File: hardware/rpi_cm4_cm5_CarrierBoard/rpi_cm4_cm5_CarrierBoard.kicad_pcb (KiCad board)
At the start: 2 copper layers, 181.6 x 100.6 mm, 489 parts, among them J1 DM3AT-SF-PEJM5, J19 RPI_CMx_A, J2 0484050003, J3 0484050003, J4 2086581001, J5 0826-1X1T-32-F, J6 M20-9990245, J7 2998TR, J8 62684-402100ALF, J9 5051101092, Q1 2N7002, Q10 SSM3K56FS,LF, Q11 SSM3K56FS,LF, Q12 2N7002, Q13 2N7002, Q14 2N7002, Q15 2N7002, Q16 BCP56-16, Q17 ISP75DP06LMXTSA1, Q18 MMBT3904-7-F, Q2 2N7002, Q3 2N7002, Q4 2N7002, Q5 2N7002, Q6 2N7002, Q7 2N7002, Q8 2N7002, Q9 IPD60R360P7ATMA1, U1 STM6710DWB6F, U10 TPS54527DDAR, U11 TPS54527DDAR, U12 TPS7A7001DDAR, U13 SE555DR, U14 SN74LVC1G14DBVR, U15 SN65DSI84ZXHR, U16 SN74LVC1G125DBVR, U17 RPI_CMx_B, U18 AP22913W6-7, U19 SN74LVC1G125DBVR, U2 SN74LVC1G125DBVR, U20 SN74LVC1G07DBVR, U21 MCP7940NT-I/MS, U22 FSUSB42UMX, U23 LTC4359IDCB, U24 MAX16928CGUP, U25 TPS79901DRVR, U26 TPS61169DCKR, U27 AP22913W6-7, U28 DSPIC33EP512MU810-I/PT, U3 SN74LVC1G125DBVR, U4 AP22913W6-7, U5 SN74LVC1G125DBVR, U6 SST25VF512A, U7 UPD720202K8-711-BAA-A, U8 AP2192AFGEG-7, U9 TPS54527DDAR, Y1 24MHz, Y2 32.768kHz

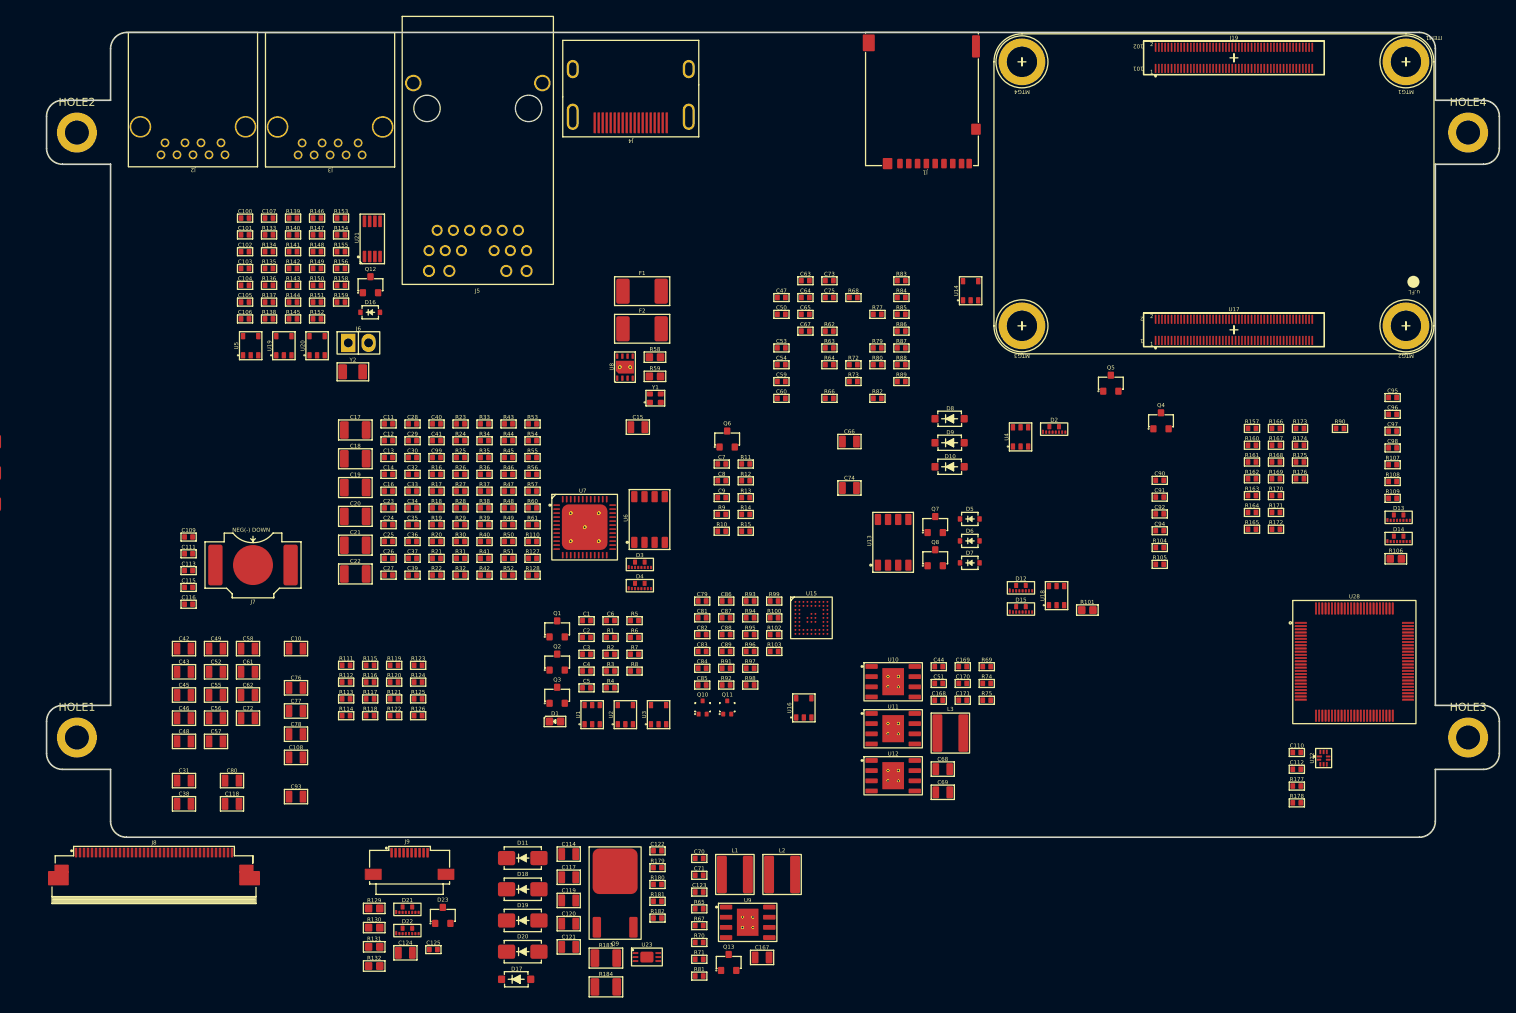
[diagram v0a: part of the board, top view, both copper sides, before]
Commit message: Add dsPIC sheet
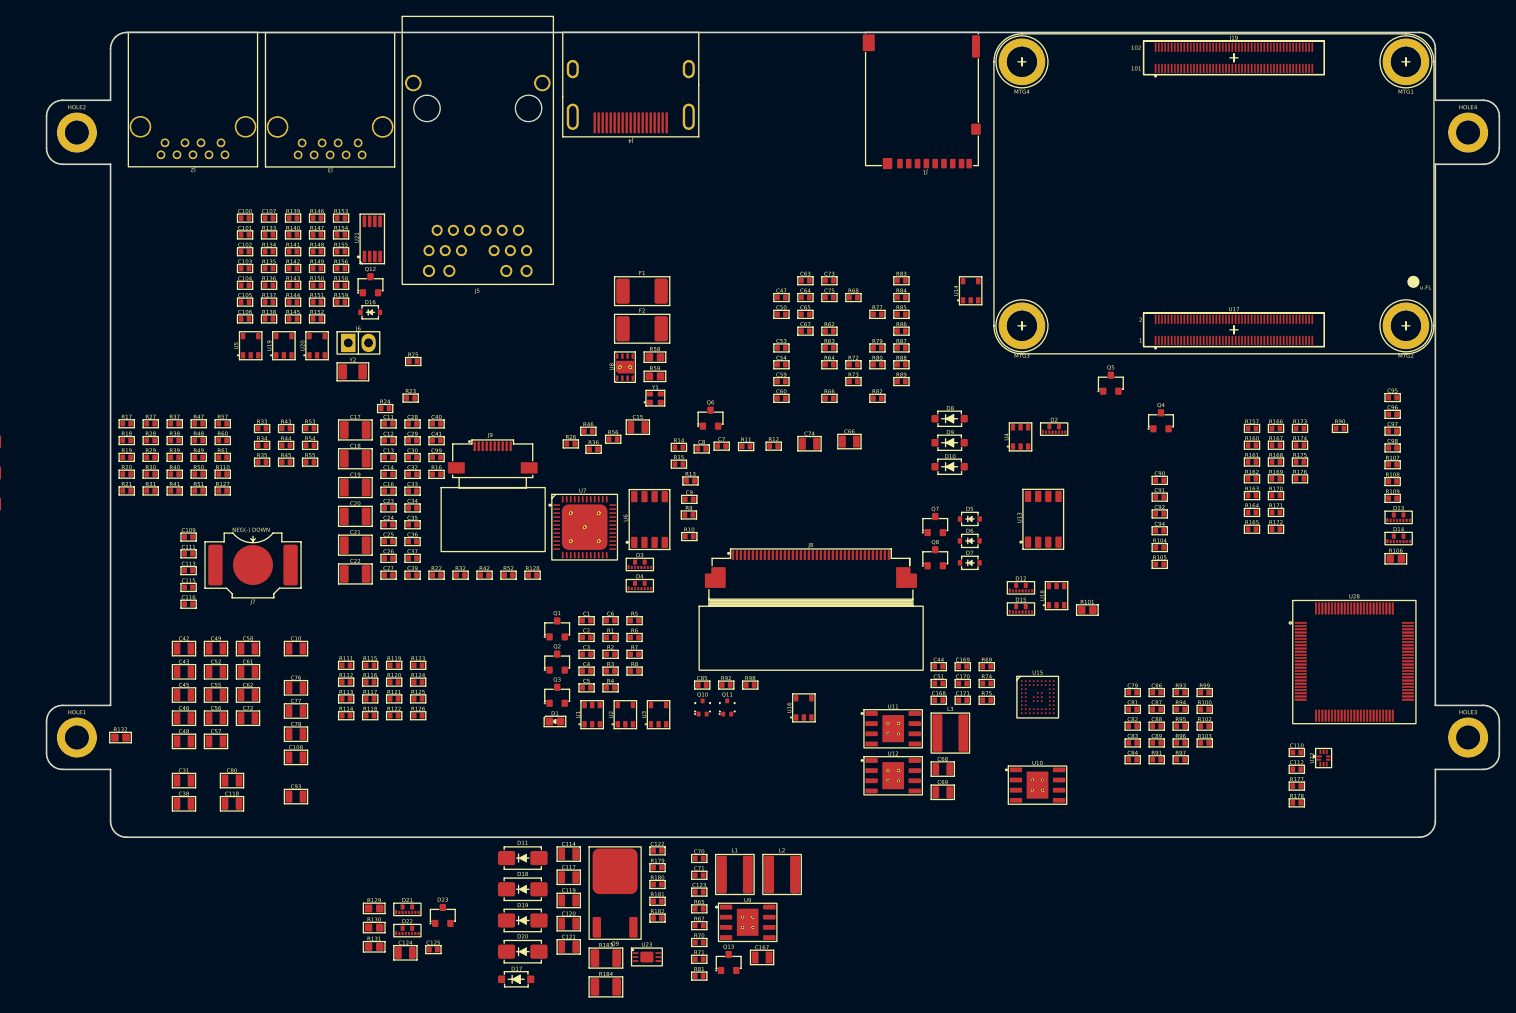
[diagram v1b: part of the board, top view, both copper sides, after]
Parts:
- added MTG**: Untitled, footprint:SLOT_TH_20_5mm, F.Cu at (155.0, 114.3)
- added MTG**: Untitled, footprint:SLOT_TH_5_5mm, F.Cu at (115.2, 99.5)
- moved J8 90.1 mm to (155.0, 106.7)
- moved C79 55.0 mm to (195.2, 121.1)
- moved C82 55.0 mm to (195.2, 125.3)
- moved C83 55.0 mm to (195.2, 127.4)
- moved C86 55.0 mm to (198.2, 121.1)
- moved C88 55.0 mm to (198.2, 125.3)
- moved C89 55.0 mm to (198.2, 127.4)
- moved R102 55.0 mm to (204.2, 125.3)
- moved R103 55.0 mm to (204.2, 127.4)
- moved R93 55.0 mm to (201.2, 121.1)
- moved R95 55.0 mm to (201.2, 125.3)
- moved R96 55.0 mm to (201.2, 127.4)
- moved R99 55.0 mm to (204.2, 121.1)
- moved C81 55.0 mm to (195.2, 123.2)
- moved C84 55.0 mm to (195.2, 129.5)
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
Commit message: Significant update to schematics Add codec, Mikrobus, PIC32A Add power table, design notes for pinmux Add datasheets
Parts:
- removed C117, C119, C120, C121: 22u, footprint:CAP_NONPOL_0805
- removed C122: 0.1u, footprint:CAP_NONPOL_0402
- removed D17: MMSZ5242B-TP, footprint:SOD-123
- removed D19: SML4761A-E3/5A, footprint:DO-214AC
- removed D20: SK34A-LTP, footprint:DO-214AC
- removed Q9: IPD60R360P7ATMA1, footprint:TO-252-3
- removed R181: 470R, footprint:RES_0402
- removed R182: 22R, footprint:RES_0402
- removed R183, R184: 0R, footprint:RES_1206
- removed U23: LTC4359IDCB, footprint:6-WFDFN-EP
- added C172: 0.1u, footprint:CAP_NONPOL_0402, F.Cu at (150.2, 47.1)
- added C173: 0.1u, footprint:CAP_NONPOL_0402, F.Cu at (150.2, 49.2)
- added C174: 0.1u, footprint:CAP_NONPOL_0402, F.Cu at (150.2, 51.3)
- added C175: 0.1u, footprint:CAP_NONPOL_0402, F.Cu at (150.2, 53.4)
- added C177: 22u, footprint:CAP_NONPOL_0805, F.Cu at (46.7, 61.5)
- added C178: 0.1u, footprint:CAP_NONPOL_0402, F.Cu at (23.8, 56.0)
- added C179: 22u, footprint:CAP_NONPOL_0805, F.Cu at (46.7, 64.4)
- added C180: 0.1u, footprint:CAP_NONPOL_0402, F.Cu at (23.8, 58.1)
- added C181: 0.1u, footprint:CAP_NONPOL_0402, F.Cu at (23.8, 60.2)
- added C182: 0.1u, footprint:CAP_NONPOL_0402, F.Cu at (23.8, 62.3)
- added C183: 0.1u, footprint:CAP_NONPOL_0402, F.Cu at (23.8, 64.4)
- added C184: 0.1u, footprint:CAP_NONPOL_0402, F.Cu at (23.8, 66.5)
- added C185: 1n, footprint:CAP_NONPOL_0402, F.Cu at (23.8, 68.6)
- added C186: 1n, footprint:CAP_NONPOL_0402, F.Cu at (23.8, 70.7)
- added C187: 1n, footprint:CAP_NONPOL_0402, F.Cu at (23.8, 72.8)
- added C188: 1n, footprint:CAP_NONPOL_0402, F.Cu at (23.8, 74.9)
- added C189: 1n, footprint:CAP_NONPOL_0402, F.Cu at (23.8, 77.0)
- added C190: 0.1u, footprint:CAP_NONPOL_0402, F.Cu at (23.8, 79.1)
- added C191: 0.1u, footprint:CAP_NONPOL_0402, F.Cu at (26.8, 56.0)
- added C192: 0.1u, footprint:CAP_NONPOL_0402, F.Cu at (26.8, 58.1)
- added C193: 0.1u, footprint:CAP_NONPOL_0402, F.Cu at (26.8, 60.2)
- added C195: 1u, footprint:CAP_NONPOL_0805, F.Cu at (53.4, 39.5)
- added C196: 10u, footprint:CAP_NONPOL_0805, F.Cu at (53.4, 42.4)
- added C197: 0.1u, footprint:CAP_NONPOL_0402, F.Cu at (52.9, 24.4)
- added C198: 10u, footprint:CAP_NONPOL_0805, F.Cu at (53.4, 45.3)
- added C199: 1u, footprint:CAP_NONPOL_0805, F.Cu at (53.4, 48.2)
- added C200: 0.1u, footprint:CAP_NONPOL_0402, F.Cu at (52.9, 26.5)
- added C201: 13p, footprint:CAP_NONPOL_0402, F.Cu at (26.8, 64.4)
- added C202: 13p, footprint:CAP_NONPOL_0402, F.Cu at (26.8, 66.5)
- added C203: 1u, footprint:CAP_NONPOL_0805, F.Cu at (244.1, 63.5)
- added C204: 1u, footprint:CAP_NONPOL_0805, F.Cu at (244.1, 66.4)
- added C205: 0.1u, footprint:CAP_NONPOL_0402, F.Cu at (247.6, 84.0)
- added C206: 0.1u, footprint:CAP_NONPOL_0402, F.Cu at (247.6, 86.1)
- added C207: 1u, footprint:CAP_NONPOL_0805, F.Cu at (244.1, 69.3)
- added C208: 1u, footprint:CAP_NONPOL_0805, F.Cu at (244.1, 72.2)
- added C209: 1u, footprint:CAP_NONPOL_0805, F.Cu at (244.1, 75.1)
- added C210: 0.1u, footprint:CAP_NONPOL_0402, F.Cu at (247.6, 88.2)
- added C211: 1u, footprint:CAP_NONPOL_0805, F.Cu at (244.1, 78.0)
- added C212: 10u, footprint:CAP_NONPOL_0805, F.Cu at (244.1, 80.9)
- added C213: 0.1u, footprint:CAP_NONPOL_0402, F.Cu at (247.6, 90.3)
- added C214: 0.1u, footprint:CAP_NONPOL_0402, F.Cu at (247.6, 92.4)
- added C215: 0.1u, footprint:CAP_NONPOL_0402, F.Cu at (247.6, 94.5)
- added C216: 0.1u, footprint:CAP_NONPOL_0402, F.Cu at (250.6, 84.0)
- added C217: 1u, footprint:CAP_NONPOL_0805, F.Cu at (244.1, 83.8)
- added C218: 0.1u, footprint:CAP_NONPOL_0402, F.Cu at (250.6, 86.1)
- added C219: 0.1u, footprint:CAP_NONPOL_0402, F.Cu at (250.6, 88.2)
- added C220: 0.1u, footprint:CAP_NONPOL_0402, F.Cu at (250.6, 90.3)
- added C221: 22u, footprint:CAP_NONPOL_0805, F.Cu at (251.7, 110.8)
- added D31: BAT42WS-TP, footprint:SOD-323, F.Cu at (42.5, 69.7)
- added D32: BAT42WS-TP, footprint:SOD-323, F.Cu at (42.5, 72.5)
- added D33: D1213A-02SOL-7, footprint:SOT-23-3, F.Cu at (42.5, 62.1)
- added D34: D1213A-02SOL-7, footprint:SOT-23-3, F.Cu at (42.5, 66.3)
- added J10: PR20206VBNN, footprint:HEADER_6P_2_54MM, F.Cu at (30.6, 82.1)
- added J11: MIKROE-4247, footprint:MIKROBUS_SOCKET_TH, F.Cu at (36.8, 38.1)
- added J12: SJ-3523-SMT-TR, footprint:SJ-352X-SMT, F.Cu at (251.9, 72.5)
- added J13: SJ-3523-SMT-TR, footprint:SJ-352X-SMT, F.Cu at (263.6, 72.5)
- added J14: SJ-3523-SMT-TR, footprint:SJ-352X-SMT, F.Cu at (275.2, 72.5)
- added J15: TB002-500-02BE, footprint:TB002-500-02BE, F.Cu at (255.2, 102.0)
- added Q19: DMPH6050SK3-13, footprint:TO-252-3, F.Cu at (245.9, 104.0)
- added R212: 0R010, footprint:RES_SENSE_1206, F.Cu at (146.0, 52.0)
- added R213: 0R010, footprint:RES_SENSE_1206, F.Cu at (146.0, 56.0)
- added R214: 0R010, footprint:RES_SENSE_1206, F.Cu at (146.0, 60.0)
- added R216: 10K, footprint:RES_0402, F.Cu at (26.8, 68.6)
- added R217: 30K1, footprint:RES_0402, F.Cu at (26.8, 70.7)
- added R218: 10K, footprint:RES_0402, F.Cu at (26.8, 72.8)
- added R219: 10K, footprint:RES_0402, F.Cu at (26.8, 74.9)
- added R220: 10K, footprint:RES_0402, F.Cu at (26.8, 77.0)
- added R221: 10K, footprint:RES_0402, F.Cu at (26.8, 79.1)
- added R222: 10K, footprint:RES_0402, F.Cu at (29.8, 56.0)
- added R223: 10K, footprint:RES_0402, F.Cu at (29.8, 58.1)
- added R224: 10K, footprint:RES_0402, F.Cu at (29.8, 60.2)
- added R225: 10K, footprint:RES_0402, F.Cu at (29.8, 62.3)
- added R226: 10K, footprint:RES_0402, F.Cu at (29.8, 64.4)
- added R227: 10K, footprint:RES_0402, F.Cu at (29.8, 66.5)
- added R228: 10K, footprint:RES_0402, F.Cu at (29.8, 68.6)
- added R229: 10K, footprint:RES_0402, F.Cu at (29.8, 70.7)
- added R230: 10K, footprint:RES_0402, F.Cu at (29.8, 72.8)
- added R231: 10K, footprint:RES_0402, F.Cu at (29.8, 74.9)
- added R233: 10K, footprint:RES_0402, F.Cu at (29.8, 79.1)
- added R234: 22R, footprint:RES_0402, F.Cu at (32.8, 56.0)
- added R235: 10K, footprint:RES_0402, F.Cu at (32.8, 58.1)
- added R236: 10K, footprint:RES_0402, F.Cu at (32.8, 60.2)
- added R237: 10K, footprint:RES_0402, F.Cu at (32.8, 62.3)
- added R238: 10K, footprint:RES_0402, F.Cu at (32.8, 64.4)
- added R239: 22R, footprint:RES_0402, F.Cu at (32.8, 66.5)
- added R240: 10K, footprint:RES_0402, F.Cu at (32.8, 68.6)
- added R241: 10K, footprint:RES_0402, F.Cu at (52.9, 28.6)
- added R242: 22R, footprint:RES_0402, F.Cu at (52.9, 30.7)
- added R243: 22R, footprint:RES_0402, F.Cu at (52.9, 32.8)
- added R244: 22R, footprint:RES_0402, F.Cu at (52.9, 34.9)
- added R245: 10K, footprint:RES_0402, F.Cu at (52.9, 37.0)
- added R246: 22R, footprint:RES_0402, F.Cu at (32.8, 70.7)
- added R247: 22R, footprint:RES_0402, F.Cu at (32.8, 72.8)
- added R248: 10K, footprint:RES_0402, F.Cu at (32.8, 74.9)
- added R249: 10K, footprint:RES_0402, F.Cu at (32.8, 77.0)
- added R250: 22R, footprint:RES_0402, F.Cu at (32.8, 79.1)
- added R251: 10K, footprint:RES_0402, F.Cu at (35.8, 56.0)
- added R252: 22R, footprint:RES_0402, F.Cu at (35.8, 58.1)
- added R253: 10K, footprint:RES_0402, F.Cu at (35.8, 60.2)
- added R254: 10K, footprint:RES_0402, F.Cu at (35.8, 62.3)
- added R255: 22R, footprint:RES_0402, F.Cu at (35.8, 64.4)
- added R256: 22R, footprint:RES_0402, F.Cu at (35.8, 66.5)
- added R257: 22R, footprint:RES_0402, F.Cu at (35.8, 68.6)
- added R258: 22R, footprint:RES_0402, F.Cu at (35.8, 70.7)
- added R259: 22R, footprint:RES_0402, F.Cu at (35.8, 72.8)
- added R260: 10K, footprint:RES_0402, F.Cu at (35.8, 74.9)
- added R261: 10K, footprint:RES_0402, F.Cu at (35.8, 77.0)
- added R262: 22R, footprint:RES_0402, F.Cu at (35.8, 79.1)
- added R263: 10K, footprint:RES_0402, F.Cu at (38.8, 56.0)
- added R264: 22R, footprint:RES_0402, F.Cu at (38.8, 58.1)
- added R265: 22R, footprint:RES_0402, F.Cu at (38.8, 60.2)
- added R266: 22R, footprint:RES_0402, F.Cu at (38.8, 62.3)
- added R267: 4K7, footprint:RES_0402, F.Cu at (38.8, 64.4)
- added R268: 4K7, footprint:RES_0402, F.Cu at (38.8, 66.5)
- added R269: 4K7, footprint:RES_0402, F.Cu at (38.8, 68.6)
- added R270: 4K7, footprint:RES_0402, F.Cu at (38.8, 70.7)
- added R271: 10K, footprint:RES_0402, F.Cu at (38.8, 72.8)
- added R272: 22R, footprint:RES_0402, F.Cu at (38.8, 74.9)
- added R273: 1Meg, footprint:RES_0402, F.Cu at (38.8, 77.0)
- added R274: 22R, footprint:RES_0402, F.Cu at (250.6, 92.4)
- added R275: 22R, footprint:RES_0402, F.Cu at (250.6, 94.5)
- added R276: 0R, footprint:RES_0402, F.Cu at (253.6, 84.0)
- added R277: 2K2, footprint:RES_0402, F.Cu at (253.6, 86.1)
- added R278: 0R, footprint:RES_0402, F.Cu at (253.6, 88.2)
- added R279: 10K, footprint:RES_0402, F.Cu at (253.6, 90.3)
- added R280: 10K, footprint:RES_0402, F.Cu at (253.6, 92.4)
- added R281: 12K, footprint:RES_0402, F.Cu at (255.2, 110.5)
- added R76: 0R, footprint:RES_0402, F.Cu at (150.8, 64.3)
- added R78: 0R010, footprint:RES_SENSE_1206, F.Cu at (146.0, 48.0)
- added S1: Y35A23310FPLFG, footprint:Y35A23310FPLFG, F.Cu at (44.9, 57.5)
- added S2: Y35A23310FPLFG, footprint:Y35A23310FPLFG, F.Cu at (267.4, 100.1)
- added U29: INA180A2IDBVR, footprint:SOT-23-5, F.Cu at (145.6, 43.7)
- added U30: INA180A2IDBVR, footprint:SOT-23-5, F.Cu at (149.7, 43.7)
- added U31: INA180A2IDBVR, footprint:SOT-23-5, F.Cu at (153.9, 43.7)
- added U32: INA180A2IDBVR, footprint:SOT-23-5, F.Cu at (158.0, 43.7)
- added U34: SGTL5000XNBA3R2, footprint:32-HPQFN, F.Cu at (258.7, 86.6)
- added U35: AP22913W6-7, footprint:SOT-23-6, F.Cu at (264.6, 85.3)
- added U36: AP22913W6-7, footprint:SOT-23-6, F.Cu at (268.7, 85.3)
- added U37: 12MHz, footprint:SOT-23-5, F.Cu at (272.9, 85.3)
- added X1: CMM-3729AT-42308-TR, footprint:CMM-3729AT-42308-TR, F.Cu at (257.1, 92.7)
- added Y3: 20MHz, footprint:4-SMD_2mmx1_6mm, F.Cu at (46.6, 69.9)
- D11: value SK34A-LTP -> SMAJ12CA
- D18: value SK34A-LTP -> MMSZ5242B-TP; footprint footprint:DO-214AC -> footprint:SOD-123
- R111: value 10K -> 22R
- R179: value 1K -> 22R
- R180: value 1K -> 10K
- R4: value 1Meg -> 10K
- U28: value DSPIC33EP512MU810-I/PT -> PIC32AK1216GC41064-I/M7; footprint footprint:TQFP-100-12x12 -> footprint:64-VQFN-EP(9x9mm)
- moved D18 142.7 mm to (256.6, 108.0)
- moved R179 134.4 mm to (264.3, 103.7)
- moved R180 134.4 mm to (264.3, 105.8)
- moved C114 131.3 mm to (251.7, 107.9)
- moved D11 130.3 mm to (245.8, 112.2)
- moved R111 67.3 mm to (53.1, 66.6)
- moved R4 58.4 mm to (145.8, 64.3)
- moved U28 13.3 mm to (210.4, 112.6), turned to 45 degrees
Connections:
- net /CM4_CM5_CONN_A/I2S_DIN renamed /AUDIO_CODEC/I2S_DIN
- net /CM4_CM5_CONN_A/dsPIC_~{INT} renamed /CM4_CM5_CONN_A/PIC_INT
- net /CM4_CM5_CONN_B/CSI1.CLK_N renamed /CM4_CM5_CONN_B/MIPI0.CLK_N
- net /CM4_CM5_CONN_B/CSI1.CLK_P renamed /CM4_CM5_CONN_B/MIPI0.CLK_P
- net /CM4_CM5_CONN_B/CSI1.D0_N renamed /CM4_CM5_CONN_B/MIPI0.D0_N
- net /CM4_CM5_CONN_B/CSI1.D0_P renamed /CM4_CM5_CONN_B/MIPI0.D0_P
- net /CM4_CM5_CONN_B/CSI1.D1_N renamed /CM4_CM5_CONN_B/MIPI0.D1_N
- net /CM4_CM5_CONN_B/CSI1.D1_P renamed /CM4_CM5_CONN_B/MIPI0.D1_P
- net /CM4_CM5_CONN_B/CSI1.D2_N renamed /CM4_CM5_CONN_B/MIPI0.D2_N
- net /CM4_CM5_CONN_B/CSI1.D2_P renamed /CM4_CM5_CONN_B/MIPI0.D2_P
- net /CM4_CM5_CONN_B/CSI1.D3_N renamed /CM4_CM5_CONN_B/MIPI0.D3_N
- net /CM4_CM5_CONN_B/CSI1.D3_P renamed /CM4_CM5_CONN_B/MIPI0.D3_P
- net /Power Supply/PWR_LOG_EN renamed /Power Supply/CB_LOG_PWR_EN
- net Net-(Q7-D) renamed /Power Supply/RPI_5V_EN
- C110 pad 2: /USB_MUX/USB.OTG_ID -> /CM4_CM5_CONN_B/USB.OTG_ID
- C114 pad 1: GND -> Net-(D18-A)
- C114 pad 2: Net-(C114-Pad2) -> Net-(D18-K)
- C40 pad 1: /USB_3/USB_HUB.RX_P -> /CM4_CM5_CONN_B/USB_HUB.RX_P
- C41 pad 1: /USB_3/USB_HUB.RX_N -> /CM4_CM5_CONN_B/USB_HUB.RX_N
- C42 pad 2: 3V3_CB -> Net-(D8-K)
- C43 pad 2: 3V3_CB -> Net-(D8-K)
- C44 pad 2: 3V3_CB -> Net-(D9-K)
- C45 pad 2: 3V3_CB -> Net-(D9-K)
- C46 pad 2: 3V3_CB -> Net-(D9-K)
- C47 pad 2: 3V3_CB -> Net-(D9-K)
- C48 pad 2: 1V05_CB -> Net-(U12-OUT)
- C49 pad 2: 1V05_CB -> Net-(U12-OUT)
- C50 pad 2: 3V3_CB -> Net-(D8-K)
- C51 pad 2: 1V8_CB -> Net-(D10-K)
- C52 pad 2: 1V8_CB -> Net-(D10-K)
- C53 pad 2: 1V05_CB -> Net-(U12-OUT)
- C57 pad 2: 12V0_CB -> Net-(D18-K)
- C58 pad 2: 12V0_CB -> Net-(D18-K)
- C59 pad 2: 12V0_CB -> Net-(D18-K)
- C65 pad 2: 12V0_CB -> Net-(D18-K)
- C71 pad 2: 3V3_CB -> Net-(D8-K)
- C72 pad 2: 1V8_CB -> Net-(D10-K)
- C73 pad 2: 1V8_CB -> Net-(D10-K)
- C74 pad 2: Net-(Q8-D) -> Net-(U13-TRIG)
- D10 pad 1: 1V8_CB -> Net-(D10-K)
- D11 pad 1: Net-(D11-K) -> GND
- D11 pad 2: Net-(D11-A) -> /Power Supply/12V_PSU
- D12 pad 1: /HDMI/HDMI0.CLK_P -> /CM4_CM5_CONN_B/HDMI0.CLK_P
- D12 pad 2: /HDMI/HDMI0.CLK_N -> /CM4_CM5_CONN_B/HDMI0.CLK_N
- D12 pad 4: /HDMI/HDMI0.SCL -> /CM4_CM5_CONN_B/HDMI0.SCL
- D12 pad 5: /HDMI/HDMI0.SDA -> /CM4_CM5_CONN_B/HDMI0.SDA
- D12 pad 7: /HDMI/HDMI0.CEC -> /CM4_CM5_CONN_B/HDMI0.CEC
- D12 pad 8: /HDMI/HDMI0.HPD -> /CM4_CM5_CONN_B/HDMI0.HPD
- D15 pad 1: /HDMI/HDMI0.D2_P -> /CM4_CM5_CONN_B/HDMI0.D2_P
- D15 pad 2: /HDMI/HDMI0.D2_N -> /CM4_CM5_CONN_B/HDMI0.D2_N
- D15 pad 4: /HDMI/HDMI0.D1_P -> /CM4_CM5_CONN_B/HDMI0.D1_P
- D15 pad 5: /HDMI/HDMI0.D1_N -> /CM4_CM5_CONN_B/HDMI0.D1_N
- D15 pad 7: /HDMI/HDMI0.D0_P -> /CM4_CM5_CONN_B/HDMI0.D0_P
- D15 pad 8: /HDMI/HDMI0.D0_N -> /CM4_CM5_CONN_B/HDMI0.D0_N
- D18 pad 1: CGND -> Net-(D18-K)
- D2 pad 1: /SD_CARD/SDIO_D2 -> /CM4_CM5_CONN_A/SDIO_D2
- D2 pad 2: /SD_CARD/SDIO_D3 -> /CM4_CM5_CONN_A/SDIO_D3
- D2 pad 4: /SD_CARD/SDIO_CMD -> /CM4_CM5_CONN_A/SDIO_CMD
- D2 pad 5: /SD_CARD/SDIO_CLK -> /CM4_CM5_CONN_A/SDIO_CLK
- D2 pad 7: /SD_CARD/SDIO_D0 -> /CM4_CM5_CONN_A/SDIO_D0
- D2 pad 8: /SD_CARD/SDIO_D1 -> /CM4_CM5_CONN_A/SDIO_D1
- D8 pad 1: 3V3_CB -> Net-(D8-K)
- D9 pad 1: 3V3_CB -> Net-(D9-K)
- J1 pad 1: /SD_CARD/SDIO_D2 -> /CM4_CM5_CONN_A/SDIO_D2
- J1 pad 2: /SD_CARD/SDIO_D3 -> /CM4_CM5_CONN_A/SDIO_D3
- J1 pad 3: /SD_CARD/SDIO_CMD -> /CM4_CM5_CONN_A/SDIO_CMD
- J1 pad 5: /SD_CARD/SDIO_CLK -> /CM4_CM5_CONN_A/SDIO_CLK
- J1 pad 7: /SD_CARD/SDIO_D0 -> /CM4_CM5_CONN_A/SDIO_D0
- J1 pad 8: /SD_CARD/SDIO_D1 -> /CM4_CM5_CONN_A/SDIO_D1
- J19 pad 34: /CM4_CM5_CONN_A/I2C3.I2C_SCL -> /I2C3.I2C_SCL
- J19 pad 37: /CM4_CM5_CONN_A/CMx_~{INT} -> /CM4_CM5_CONN_A/CMx_INT
- J19 pad 46: /CM4_CM5_CONN_A/RTCC -> /CM4_CM5_CONN_A/GPIO22
- J19 pad 54: /CM4_CM5_CONN_A/I2C3.I2C_SDA -> /I2C3.I2C_SDA
- J4 pad 1: /HDMI/HDMI0.D2_P -> /CM4_CM5_CONN_B/HDMI0.D2_P
- J4 pad 10: /HDMI/HDMI0.CLK_P -> /CM4_CM5_CONN_B/HDMI0.CLK_P
- J4 pad 12: /HDMI/HDMI0.CLK_N -> /CM4_CM5_CONN_B/HDMI0.CLK_N
- J4 pad 13: /HDMI/HDMI0.CEC -> /CM4_CM5_CONN_B/HDMI0.CEC
- J4 pad 15: /HDMI/HDMI0.SCL -> /CM4_CM5_CONN_B/HDMI0.SCL
- J4 pad 16: /HDMI/HDMI0.SDA -> /CM4_CM5_CONN_B/HDMI0.SDA
- J4 pad 19: /HDMI/HDMI0.HPD -> /CM4_CM5_CONN_B/HDMI0.HPD
- J4 pad 3: /HDMI/HDMI0.D2_N -> /CM4_CM5_CONN_B/HDMI0.D2_N
- J4 pad 4: /HDMI/HDMI0.D1_P -> /CM4_CM5_CONN_B/HDMI0.D1_P
- J4 pad 6: /HDMI/HDMI0.D1_N -> /CM4_CM5_CONN_B/HDMI0.D1_N
- J4 pad 7: /HDMI/HDMI0.D0_P -> /CM4_CM5_CONN_B/HDMI0.D0_P
- J4 pad 9: /HDMI/HDMI0.D0_N -> /CM4_CM5_CONN_B/HDMI0.D0_N
- L1 pad 2: 3V3_CB -> Net-(D8-K)
- L2 pad 2: 3V3_CB -> Net-(D9-K)
- L3 pad 2: 1V8_CB -> Net-(D10-K)
- Q1 pad 1: unconnected-(Q1-G-Pad1) -> /RESET_SUPERVISOR/PWG
- Q1 pad 3: /RESET_SUPERVISOR/PWG -> Net-(Q1-D)
- Q10 pad 3: /DSI - LVDS bridge/I2C3.I2C_SDA -> /I2C3.I2C_SDA
- Q11 pad 3: /DSI - LVDS bridge/I2C3.I2C_SCL -> /I2C3.I2C_SCL
- Q14 pad 1: /TFT_POWER/SYS_~{RST} -> /SYS_~{RST}
- Q2 pad 1: /RESET_SUPERVISOR/EXT_~{RST} -> /CM4_CM5_CONN_A/EXT_~{RST}
- Q3 pad 1: /RESET_SUPERVISOR/PWG -> Net-(Q1-D)
- Q4 pad 1: /SD_CARD/SD_PWR_ON -> /CM4_CM5_CONN_A/SD_PWR_ON
- R100 pad 2: /DSI - LVDS bridge/SYS_~{RST} -> /SYS_~{RST}
- R102 pad 1: /DSI - LVDS bridge/I2C3.I2C_SDA -> /I2C3.I2C_SDA
- R104 pad 2: /HDMI/SYS_~{RST} -> /SYS_~{RST}
- R110 pad 1: /USB_3/USB_HUB_~{RST} -> /SYS_~{RST}
- R111 pad 1: GND -> /CM4_CM5_CONN_A/GPIO22
- R111 pad 2: /CM4_CM5_CONN_A/RTCC -> unconnected-(R111-Pad2)
- R115 pad 2: /CM4_CM5_CONN_A/I2S_DOUT -> /AUDIO_CODEC/I2S_DOUT
- R119 pad 1: /CM4_CM5_CONN_A/CMx_~{INT} -> GND
- R119 pad 2: 3V3_CB -> /CM4_CM5_CONN_A/CMx_INT
- R122 pad 2: /CM4_CM5_CONN_A/CM5_USB3_1_~{OC} -> /CM5_USB3_1_~{OC}
- R123 pad 2: /CM4_CM5_CONN_A/CM5_USB3_0_~{OC} -> /CM5_USB3_0_~{OC}
- R125 pad 2: /CM4_CM5_CONN_A/I2S_SCLK -> /AUDIO_CODEC/I2S_SCLK
- R127 pad 1: /USB_3/CM5_USB3_0_~{OC} -> /CM5_USB3_0_~{OC}
- R128 pad 1: /USB_3/CM5_USB3_1_~{OC} -> /CM5_USB3_1_~{OC}
- R141 pad 2: /CM4_CM5_CONN_A/I2S_COFS -> /AUDIO_CODEC/I2S_COFS
- R144 pad 1: /CM4_CM5_CONN_A/I2C3.I2C_SCL -> /I2C3.I2C_SCL
- R145 pad 1: /CM4_CM5_CONN_A/I2C3.I2C_SDA -> /I2C3.I2C_SDA
- R177 pad 1: /USB_MUX/USB.OTG_ID -> /CM4_CM5_CONN_B/USB.OTG_ID
- R178 pad 2: /USB_MUX/USB.OTG_ID -> /CM4_CM5_CONN_B/USB.OTG_ID
- R179 pad 1: Net-(D19-K) -> Net-(U28B-RB2)
- R179 pad 2: Net-(D11-K) -> /PIC32AK1216/~{BTN1}
- R180 pad 1: Net-(U23-~{SHDN}) -> /PIC32AK1216/~{BTN1}
- R180 pad 2: Net-(D11-A) -> 3V3_CB
- R185 pad 2: /TFT_POWER/SYS_~{RST} -> /SYS_~{RST}
- R208 pad 2: /TFT_POWER/BL_PWM -> /CM4_CM5_CONN_A/PWM_0
- R32 pad 1: /USB_3/CM5_USB3_1.U3RXD_N -> /CM4_CM5_CONN_B/CM5_USB3_1.U3RXD_N
- R33 pad 1: /USB_3/CM5_USB3_1.U3RXD_P -> /CM4_CM5_CONN_B/CM5_USB3_1.U3RXD_P
- R34 pad 1: /USB_3/CM5_USB3_1.USB_N -> /CM4_CM5_CONN_B/CM5_USB3_1.USB_N
- R35 pad 1: /USB_3/CM5_USB3_1.USB_P -> /CM4_CM5_CONN_B/CM5_USB3_1.USB_P
- R36 pad 1: /USB_3/CM5_USB3_1.U3TXD_N -> /CM4_CM5_CONN_B/CM5_USB3_1.U3TXD_N
- R37 pad 1: /USB_3/CM5_USB3_1.U3TXD_P -> /CM4_CM5_CONN_B/CM5_USB3_1.U3TXD_P
- R38 pad 1: /USB_3/CM5_USB3_0.U3RXD_N -> /CM4_CM5_CONN_B/CM5_USB3_0.U3RXD_N
- R39 pad 1: /USB_3/CM5_USB3_0.U3RXD_P -> /CM4_CM5_CONN_B/CM5_USB3_0.U3RXD_P
- R4 pad 1: /RESET_SUPERVISOR/EXT_~{RST} -> GND
- R4 pad 2: GND -> /CM4_CM5_CONN_A/EXT_~{RST}
- R40 pad 1: /USB_3/CM5_USB3_0.USB_N -> /CM4_CM5_CONN_B/CM5_USB3_0.USB_N
- R41 pad 1: /USB_3/CM5_USB3_0.USB_P -> /CM4_CM5_CONN_B/CM5_USB3_0.USB_P
- R42 pad 1: /USB_3/CM5_USB3_0.U3TXD_N -> /CM4_CM5_CONN_B/CM5_USB3_0.U3TXD_N
- R43 pad 1: /USB_3/CM5_USB3_0.U3TXD_P -> /CM4_CM5_CONN_B/CM5_USB3_0.U3TXD_P
- R5 pad 1: /RESET_SUPERVISOR/PWG -> Net-(Q1-D)
- R61 pad 2: /USB_3/USB_HUB.~{WAKE} -> /CM4_CM5_CONN_B/USB_HUB.~{WAKE}
- R68 pad 2: 3V3_CB -> Net-(D9-K)
- R70 pad 2: 3V3_CB -> Net-(D8-K)
- R71 pad 1: Net-(Q13-D) -> Net-(D7-K)
- R72 pad 2: 3V3_CB -> Net-(D8-K)
- R73 pad 2: 3V3_CB -> Net-(D9-K)
- R75 pad 2: 1V8_CB -> Net-(D10-K)
- R77 pad 2: 1V8_CB -> Net-(D10-K)
- R79 pad 2: 12V0_CB -> Net-(D18-K)
- R8 pad 2: /RESET_SUPERVISOR/SYS_~{RST} -> /SYS_~{RST}
- R80 pad 2: 1V05_CB -> Net-(U12-OUT)
- R81 pad 2: 1V05_CB -> Net-(U12-OUT)
- R84 pad 2: 12V0_CB -> Net-(D18-K)
- R85 pad 2: 12V0_CB -> Net-(D18-K)
- R86 pad 1: Net-(Q8-D) -> Net-(U13-TRIG)
- R86 pad 2: 12V0_CB -> Net-(D18-K)
- R87 pad 2: Net-(Q8-D) -> Net-(U13-TRIG)
- R9 pad 1: /SD_CARD/SD_PWR_ON -> /CM4_CM5_CONN_A/SD_PWR_ON
- R98 pad 1: /DSI - LVDS bridge/I2C3.I2C_SCL -> /I2C3.I2C_SCL
- U12 pad 6: 1V05_CB -> Net-(U12-OUT)
- U13 pad 2: Net-(Q8-D) -> Net-(U13-TRIG)
- U13 pad 8: 12V0_CB -> Net-(D18-K)
- U16 pad 2: /DSI - LVDS bridge/SYS_~{RST} -> /SYS_~{RST}
- U17 pad 11: /CM4_CM5_CONN_B/CM5_USB3_VBUS_EN -> /USB_3/CM5_USB3_VBUS_EN
- U18 pad 3: /HDMI/SYS_~{RST} -> /SYS_~{RST}
- U21 pad 5: /CM4_CM5_CONN_A/I2C3.I2C_SDA -> /I2C3.I2C_SDA
- U21 pad 6: /CM4_CM5_CONN_A/I2C3.I2C_SCL -> /I2C3.I2C_SCL
- U22 pad 1: /USB_MUX/USB.USB_P -> /CM4_CM5_CONN_B/USB.USB_P
- U22 pad 10: /USB_MUX/USB.OTG_ID -> /CM4_CM5_CONN_B/USB.OTG_ID
- U22 pad 2: /USB_MUX/USB.USB_N -> /CM4_CM5_CONN_B/USB.USB_N
- U22 pad 4: /USB_MUX/USB_HOST.USB_N -> /TFT_CONN/USB_HOST.USB_N
- U22 pad 5: /USB_MUX/USB_HOST.USB_P -> /TFT_CONN/USB_HOST.USB_P
- U26 pad 4: /TFT_POWER/BL_PWM -> /CM4_CM5_CONN_A/PWM_0
- U28 pad 1: unconnected-(U28G-RG15-Pad1) -> /PIC32AK1216/LED1
- U28 pad 10: unconnected-(U28G-RG6-Pad10) -> GND
- U28 pad 11: unconnected-(U28G-RG7-Pad11) -> 3V3_CB
- U28 pad 12: unconnected-(U28G-RG8-Pad12) -> Net-(U28A-RA2)
- U28 pad 13: unconnected-(U28H-~{MCLR}-Pad13) -> Net-(U28A-RA3)
- U28 pad 14: unconnected-(U28G-RG9-Pad14) -> Net-(U28A-RA4)
- U28 pad 15: unconnected-(U28H-VSS-Pad15) -> Net-(U28A-RA5)
- U28 pad 16: unconnected-(U28H-VDD-Pad16) -> Net-(U28A-RA6)
- U28 pad 17: unconnected-(U28A-RA0-Pad17) -> Net-(U28B-RB5)
- U28 pad 18: unconnected-(U28E-RE8-Pad18) -> GND
- U28 pad 19: unconnected-(U28E-RE9-Pad19) -> 3V3_CB
- U28 pad 2: unconnected-(U28H-VDD-Pad2) -> Net-(U28A-RA7)
- U28 pad 20: unconnected-(U28B-RB5-Pad20) -> Net-(U28B-RB0)
- U28 pad 21: unconnected-(U28B-RB4-Pad21) -> Net-(U28B-RB1*)
- U28 pad 22: unconnected-(U28B-RB3-Pad22) -> Net-(U28B-RB2)
- U28 pad 23: unconnected-(U28B-RB2-Pad23) -> Net-(U28B-RB8)
- U28 pad 24: unconnected-(U28B-RB1-Pad24) -> /PIC32AK1216/WDOG_IN
- U28 pad 25: unconnected-(U28B-RB0-Pad25) -> GND
- U28 pad 26: unconnected-(U28B-RB6-Pad26) -> 3V3_CB
- U28 pad 27: unconnected-(U28B-RB7-Pad27) -> Net-(U28E-ICSPDAT)
- U28 pad 28: unconnected-(U28A-RA9-Pad28) -> Net-(D33-A)
- U28 pad 29: unconnected-(U28A-RA10-Pad29) -> Net-(U28B-RB6)
- U28 pad 3: unconnected-(U28E-RE5-Pad3) -> Net-(U28A-RA1)
- U28 pad 30: unconnected-(U28H-AVDD-Pad30) -> Net-(U28B-RB7)
- U28 pad 31: unconnected-(U28H-AVSS-Pad31) -> /PIC32AK1216/SPI2.MISO
- U28 pad 32: unconnected-(U28B-RB8-Pad32) -> /PIC32AK1216/SPI2.MISO
- U28 pad 33: unconnected-(U28B-RB9-Pad33) -> /PIC32AK1216/SPI2.MISO
- U28 pad 34: unconnected-(U28B-RB10-Pad34) -> Net-(U28C-RC9)
- U28 pad 35: unconnected-(U28B-RB11-Pad35) -> Net-(U28C-RC6)
- U28 pad 36: unconnected-(U28H-VSS-Pad36) -> /PIC32AK1216/MKB1.AN
- U28 pad 37: unconnected-(U28H-VDD-Pad37) -> Net-(U28E-OSCO)
- U28 pad 38: unconnected-(U28A-RA1-Pad38) -> Net-(U28E-OSC1)
- U28 pad 39: unconnected-(U28F-RF13-Pad39) -> GND
- U28 pad 4: unconnected-(U28E-RE6-Pad4) -> GND
- U28 pad 40: unconnected-(U28F-RF12-Pad40) -> 3V3_CB
- U28 pad 41: unconnected-(U28B-RB12-Pad41) -> /PIC32AK1216/MKB1.AN
- U28 pad 42: unconnected-(U28B-RB13-Pad42) -> /PIC32AK1216/MKB1.AN
- U28 pad 43: unconnected-(U28B-RB14-Pad43) -> Net-(U28C-RC3)
- U28 pad 44: unconnected-(U28B-RB15-Pad44) -> /PIC32AK1216/MKB1.AN
- U28 pad 45: unconnected-(U28H-VSS-Pad45) -> Net-(U28C-RC10)
- U28 pad 46: unconnected-(U28H-VDD-Pad46) -> Net-(U28C-RC11)
- U28 pad 47: unconnected-(U28D-RD14-Pad47) -> GND
- U28 pad 48: unconnected-(U28D-RD15-Pad48) -> 3V3_CB
- U28 pad 49: unconnected-(U28F-RF4-Pad49) -> Net-(U28D-RD9)
- U28 pad 5: unconnected-(U28E-RE7-Pad5) -> 3V3_CB
- U28 pad 50: unconnected-(U28F-RF5-Pad50) -> /PIC32AK1216/CM4_~{CM5}_BUILD
- U28 pad 51: unconnected-(U28F-RF3-Pad51) -> /PIC32AK1216/MKB1.AN
- U28 pad 52: unconnected-(U28F-RF2-Pad52) -> Net-(U28D-RD1)
- U28 pad 53: unconnected-(U28F-RF8-Pad53) -> Net-(U28D-RD2)
- U28 pad 54: unconnected-(U28H-VBUS-Pad54) -> Net-(U28D-RD3)
- U28 pad 55: unconnected-(U28H-VUSB3V3-Pad55) -> /PIC32AK1216/MKB1.AN
- U28 pad 56: unconnected-(U28G-RG3-Pad56) -> /PIC32AK1216/MKB1.AN
- U28 pad 57: unconnected-(U28G-RG2-Pad57) -> /PIC32AK1216/EXP.IO_1
- U28 pad 58: unconnected-(U28A-RA2-Pad58) -> /PIC32AK1216/EXP.IO_1
- U28 pad 59: unconnected-(U28A-RA3-Pad59) -> GND
- U28 pad 6: unconnected-(U28C-RC1-Pad6) -> /PIC32AK1216/MKB1.AN
- U28 pad 60: unconnected-(U28A-RA4-Pad60) -> 3V3_CB
- U28 pad 61: unconnected-(U28A-RA5-Pad61) -> Net-(U28D-RD4)
- U28 pad 62: unconnected-(U28H-VDD-Pad62) -> /PIC32AK1216/PIC_DBG_RXD
- U28 pad 63: unconnected-(U28H-OSC1-Pad63) -> Net-(U28D-RD12)
- U28 pad 64: unconnected-(U28H-OSC2-Pad64) -> Net-(D31-A)
- U28 pad 65: unconnected-(U28H-VSS-Pad65) -> GND
- U28 pad 7: unconnected-(U28C-RC2-Pad7) -> /PIC32AK1216/LED2
- U28 pad 8: unconnected-(U28C-RC3-Pad8) -> Net-(U28A-RA9)
- U28 pad 9: unconnected-(U28C-RC4-Pad9) -> /PIC32AK1216/PIC_INT
- U7 pad 1: /USB_3/USB_HUB.CLK_P -> /CM4_CM5_CONN_B/USB_HUB.CLK_P
- U7 pad 11: /USB_3/USB_HUB_~{RST} -> /SYS_~{RST}
- U7 pad 2: /USB_3/USB_HUB.CLK_N -> /CM4_CM5_CONN_B/USB_HUB.CLK_N
- U7 pad 47: /USB_3/USB_HUB.~{RST} -> /CM4_CM5_CONN_B/USB_HUB.~{RST}
- U7 pad 48: /USB_3/USB_HUB.~{WAKE} -> /CM4_CM5_CONN_B/USB_HUB.~{WAKE}
- U7 pad 7: /USB_3/USB_HUB.TX_P -> /CM4_CM5_CONN_B/USB_HUB.TX_P
- U7 pad 8: /USB_3/USB_HUB.TX_N -> /CM4_CM5_CONN_B/USB_HUB.TX_N
- U9 pad 8: 12V0_CB -> Net-(D18-K)

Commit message: Slight update to hierarchical top sheet
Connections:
- D5 pad 2: /Power Supply/RUN_PG -> /CM4_CM5_CONN_A/RUN_PG
- R88 pad 1: /Power Supply/POWER_KILL -> /PIC32AK1216/POWER_KILL
- R89 pad 2: /Power Supply/POWER_KILL -> /PIC32AK1216/POWER_KILL
- U29 pad 1: /Power Supply/I_5V0_CB -> /PIC32AK1216/I_5V0_CB
- U30 pad 1: /Power Supply/I_3V3_CB -> /PIC32AK1216/I_3V3_CB
- U31 pad 1: /Power Supply/I_1V8_CB -> /PIC32AK1216/I_1V8_CB
- U32 pad 1: /Power Supply/I_1V05_CB -> /PIC32AK1216/I_1V05_CB
